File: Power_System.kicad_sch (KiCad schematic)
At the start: 21 parts, among them J1 Conn_01x02, U1 LM2596S-12, U2 LM2596S-5, U3 AMS1117-3.3

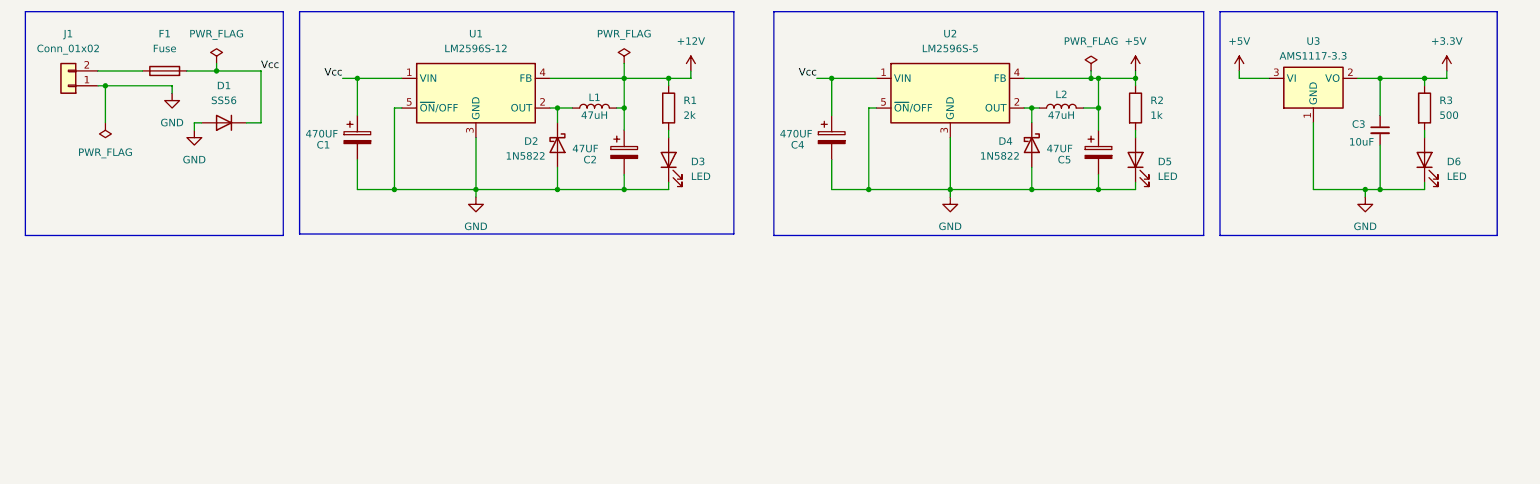
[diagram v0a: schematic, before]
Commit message: ESP32 P4 with 8 Ethernet
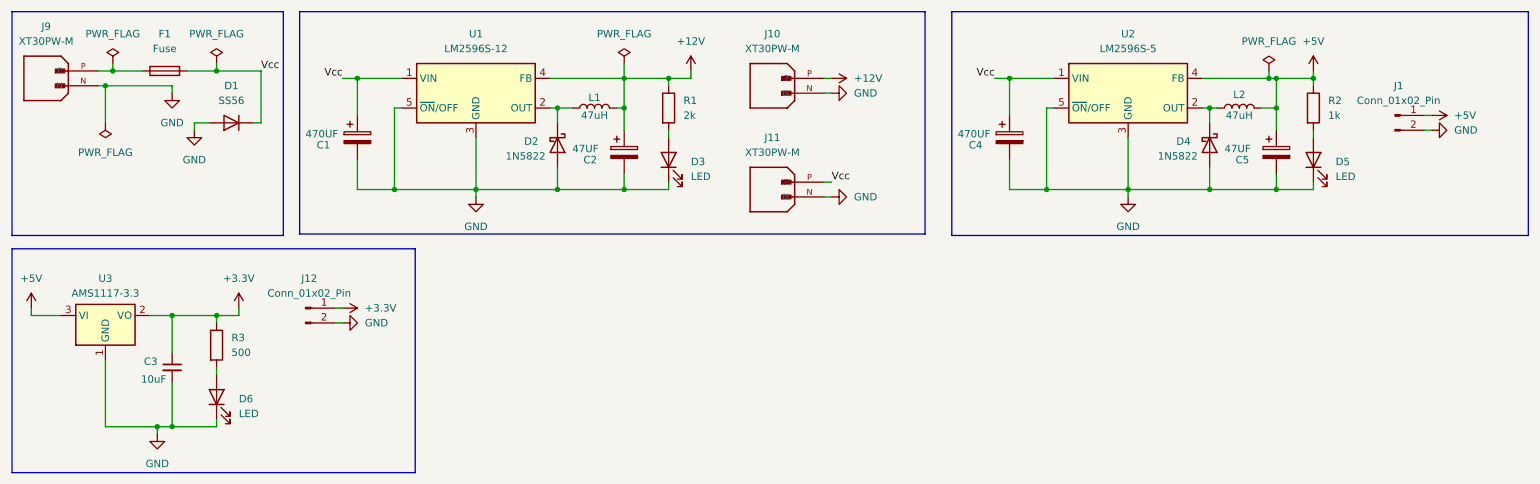
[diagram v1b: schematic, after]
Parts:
- removed J1: Conn_01x02, symbol Connector_Generic:Conn_01x02
- added J1, J12: Conn_01x02_Pin, Connector_JST:JST_PH_B2B-PH-K_1x02_P2.00mm_Vertical, symbol Connector:Conn_01x02_Pin
- added J10, J11, J9: XT30PW-M, Custom_Footprint:AMASS_XT30PW-M, symbol XT30PW-M:XT30PW-M
- D1: footprint (none) -> Diode_SMD:D_SMA
- D3, D5, D6: footprint (none) -> LED_SMD:LED_0603_1608Metric
- L1, L2: footprint (none) -> Inductor_SMD:L_Wuerth_HCI-7030
- R1, R2, R3: footprint (none) -> Resistor_SMD:R_0603_1608Metric
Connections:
- net +12V: now also J10.P
- net +3.3V: now also J12.1 (Pin_1)
- net +5V: now also J1.1 (Pin_1)
- net GND: now also J1.2 (Pin_2), J10.N, J11.N, J12.2 (Pin_2), J9.N
- net Vcc: now also J11.P
- net at F1.1: now also J9.P
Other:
- moved on the sheet: C3, C4, C5, D1, D4, D5, D6, L2, R2, R3, U2, U3
